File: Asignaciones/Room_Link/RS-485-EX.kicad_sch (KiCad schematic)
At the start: 0 parts

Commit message: ROOM-LINK update KICAD
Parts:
- added D10: LED, LED_SMD:LED_0805_2012Metric_Pad1.15x1.40mm_HandSolder, symbol Device:LED
- added D11: SM712-02HTG, sm712:SM71202HTG, symbol SM712-02HTG:SM712-02HTG
- added D12: SMBJ12CA, nuevo simbolo:SMBJ12CA, symbol SMBJ12CA:SMBJ12CA
- added F1, F2: PTS120660V010, PTS12066V050:FUSC3216X68N, symbol nuevos simvolos:PTS120660V010
- added R22, R23, R24: 2.2k, Resistor_SMD:R_0805_2012Metric_Pad1.20x1.40mm_HandSolder, symbol Device:R
- added R25, R26: 10, Resistor_SMD:R_0805_2012Metric_Pad1.20x1.40mm_HandSolder, symbol Device:R
- added U2: TD521D485H-E, nuevo simbolo:TD521D485H-E, symbol TD521D485:TD521D485
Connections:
- net CON-A-: now also F2.2
- net CON-B+: now also F1.2
- net CON_RS485_eXT: now also U2.5 (CON)
- net RGND: now also D11.3
- net Rx_RS485_eXT: now also U2.4 (RXD)
- net Tx_RS485_eXT: now also U2.3 (TXD)
- new net: F2.1, R26.2
- new net: D11.1, D12.2, R24.2, R25.1, U2.8 (B)
- new net: F1.1, R25.2
- new net: R24.1, U2.10 (RGND)
- new net: R22.1, R23.1, U2.7 (VO)
- new net: D10.1 (K), D11.2, D12.1, R23.2, R26.1, U2.9 (A)
- new net: D10.2 (A), R22.2
- new net +5V: U2.2 (GND)
- new net GND: U2.1 (VCC)

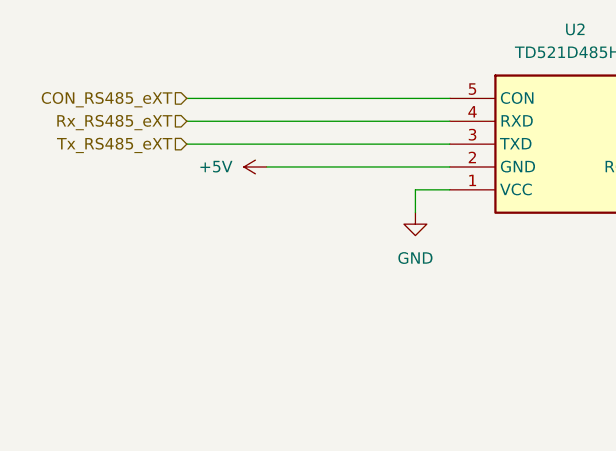
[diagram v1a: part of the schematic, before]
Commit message: Place component Added & routing
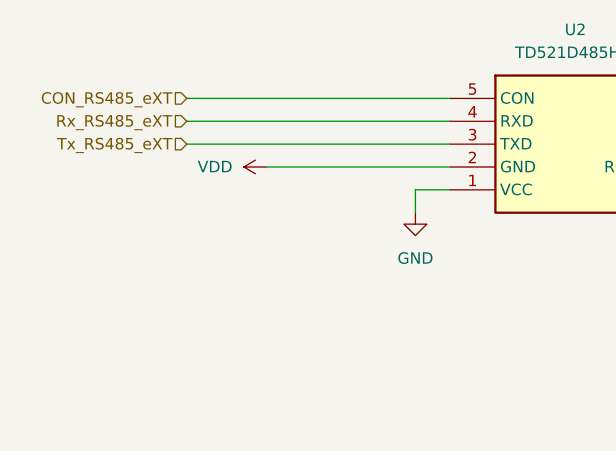
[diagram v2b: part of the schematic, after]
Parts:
- D10: footprint LED_SMD:LED_0805_2012Metric_Pad1.15x1.40mm_HandSolder -> LED_SMD:LED_0805_2012Metric
- D11: footprint sm712:SM71202HTG -> Package_TO_SOT_SMD:SOT-23
- R22, R23, R24, R25, R26: footprint Resistor_SMD:R_0805_2012Metric_Pad1.20x1.40mm_HandSolder -> Resistor_SMD:R_0805_2012Metric
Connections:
- net +5V renamed VDD
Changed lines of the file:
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@@
       (effects (font (size 1.27 1.27)))
     )
-    (property "Footprint" "Resistor_SMD:R_0805_2012Metric_Pad1.20x1.40mm_HandSolder" (at 203.2 99.568 90)
+    (property "Footprint" "Resistor_SMD:R_0805_2012Metric" (at 203.2 99.568 90)
       (effects (font (size 1.27 1.27)) hide)
     )
@@
       (effects (font (size 1.27 1.27)))
     )
-    (property "Footprint" "Resistor_SMD:R_0805_2012Metric_Pad1.20x1.40mm_HandSolder" (at 203.2 124.968 90)
+    (property "Footprint" "Resistor_SMD:R_0805_2012Metric" (at 203.2 124.968 90)
       (effects (font (size 1.27 1.27)) hide)
     )
@@
         (path "/c4ebd78f-0c54-42fb-8411-155772684713/6ffab1c0-a902-4896-acce-96f8f8ea2f51/c38d9ed4-fd09-4498-bcb3-6c7dfb3c5f4c"
           (reference "R26") (unit 1)
+        )
+      )
+    )
+  )
+  (symbol (lib_id "power:VDD") (at 67.31 102.87 90) (unit 1)
+    (in_bom yes) (on_board yes) (dnp no) (fields_autoplaced)
+    (property "Reference" "#PWR032" (at 71.12 102.87 0)
+      (effects (font (size 1.27 1.27)) hide)
+    )
+    (property "Value" "VDD" (at 63.5 102.87 90)
+      (effects (font (size 1.27 1.27)) (justify left))
+    )
+    (property "Footprint" "" (at 67.31 102.87 0)
+      (effects (font (size 1.27 1.27)) hide)
+    )
+    (property "Datasheet" "" (at 67.31 102.87 0)
+      (effects (font (size 1.27 1.27)) hide)
+    )
+    (pin "1")
+    (instances
+      (project "Room_Link"
+        (path "/c4ebd78f-0c54-42fb-8411-155772684713/6ffab1c0-a902-4896-acce-96f8f8ea2f51/c38d9ed4-fd09-4498-bcb3-6c7dfb3c5f4c"
+          (reference "#PWR032") (unit 1)
         )
       )
@@
       (effects (font (size 1.27 1.27)) (justify left))
     )
-    (property "Footprint" "sm712:SM71202HTG" (at 271.45 146.05 0)
+    (property "Footprint" "Package_TO_SOT_SMD:SOT-23" (at 271.45 146.05 0)
       (effects (font (size 1.27 1.27)) (justify left top) hide)
     )
@@
       (effects (font (size 1.27 1.27)))
     )
-    (property "Footprint" "Resistor_SMD:R_0805_2012Metric_Pad1.20x1.40mm_HandSolder" (at 128.27 104.648 90)
+    (property "Footprint" "Resistor_SMD:R_0805_2012Metric" (at 128.27 104.648 90)
       (effects (font (size 1.27 1.27)) hide)
     )
@@
       (effects (font (size 1.27 1.27)))
     )
-    (property "Footprint" "Resistor_SMD:R_0805_2012Metric_Pad1.20x1.40mm_HandSolder" (at 139.7 97.028 90)
+    (property "Footprint" "Resistor_SMD:R_0805_2012Metric" (at 139.7 97.028 90)
       (effects (font (size 1.27 1.27)) hide)
     )
@@
       (effects (font (size 1.27 1.27)))
     )
-    (property "Footprint" "LED_SMD:LED_0805_2012Metric_Pad1.15x1.40mm_HandSolder" (at 152.4 95.25 0)
+    (property "Footprint" "LED_SMD:LED_0805_2012Metric" (at 152.4 95.25 0)
       (effects (font (size 1.27 1.27)) hide)
     )
@@
       (effects (font (size 1.27 1.27)))
     )
-    (property "Footprint" "Resistor_SMD:R_0805_2012Metric_Pad1.20x1.40mm_HandSolder" (at 125.73 95.758 90)
+    (property "Footprint" "Resistor_SMD:R_0805_2012Metric" (at 125.73 95.758 90)
       (effects (font (size 1.27 1.27)) hide)
     )
@@
         )
       )
-    )
-  )
-  (symbol (lib_id "power:+5V") (at 67.31 102.87 90) (unit 1)
-    (in_bom yes) (on_board yes) (dnp no) (fields_autoplaced)
-    (property "Reference" "#PWR032" (at 71.12 102.87 0)
-      (effects (font (size 1.27 1.27)) hide)
-    )
-    (property "Value" "+5V" (at 63.5 102.87 90)
-      (effects (font (size 1.27 1.27)) (justify left))
-    )
-    (property "Footprint" "" (at 67.31 102.87 0)
-      (effects (font (size 1.27 1.27)) hide)
-    )
-    (property "Datasheet" "" (at 67.31 102.87 0)
-      (effects (font (size 1.27 1.27)) hide)
-    )
-    (pin "1")
-    (instances
-      (project "Room_Link"
-        (path "/c4ebd78f-0c54-42fb-8411-155772684713/6ffab1c0-a902-4896-acce-96f8f8ea2f51/c38d9ed4-fd09-4498-bcb3-6c7dfb3c5f4c"
-          (reference "#PWR032") (unit 1)
-        )
-      )
